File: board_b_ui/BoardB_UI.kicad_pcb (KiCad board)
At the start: 2 copper layers, 64 x 38 mm, 17 parts, among them J1 UI cable to Board A J6, J2 OLED SSD1306 I2C, SW1 EC11 encoder + push

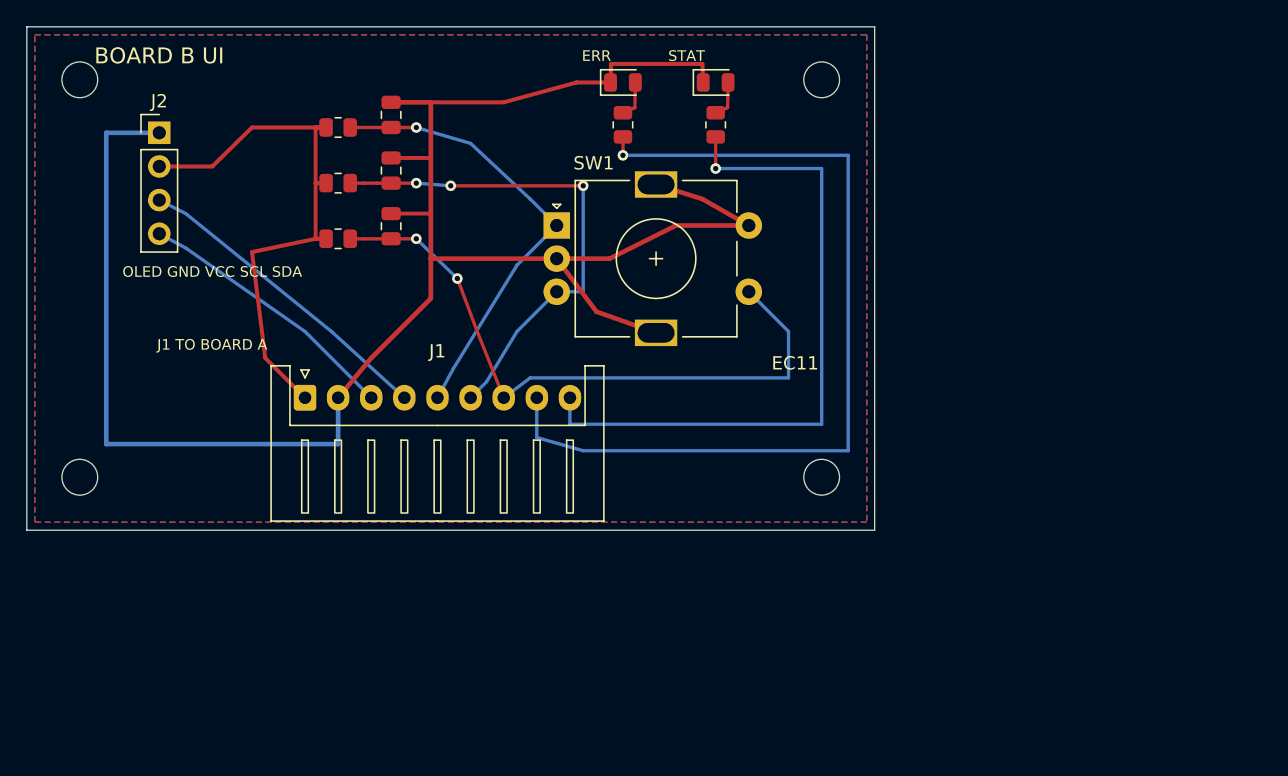
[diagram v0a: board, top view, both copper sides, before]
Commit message: Add Board B fab package and Board A hold report
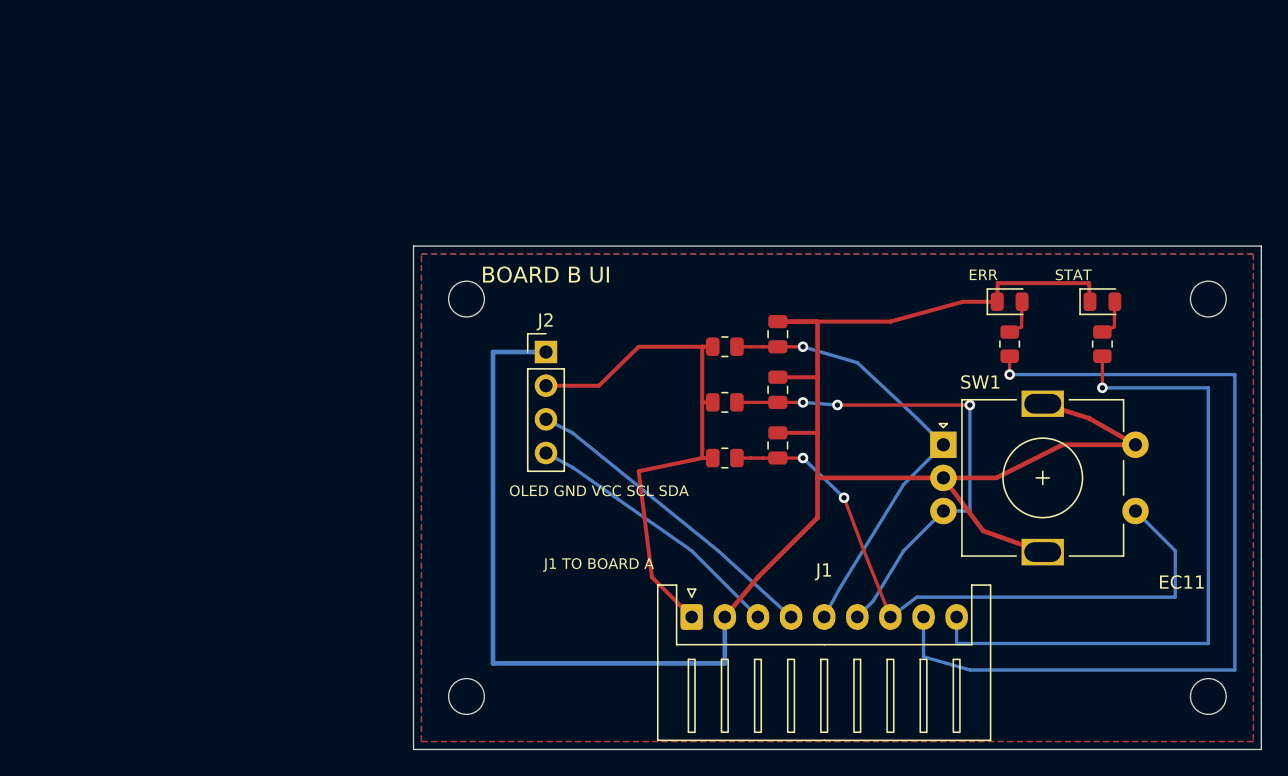
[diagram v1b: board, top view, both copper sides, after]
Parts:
- moved C1 33.6 mm to (56.7, 23.2)
- moved C2 33.6 mm to (56.7, 27.4)
- moved C3 33.6 mm to (56.7, 31.6)
- moved D1 33.6 mm to (74.2, 20.8)
- moved D2 33.6 mm to (81.2, 20.8)
- moved H1 33.6 mm to (33.2, 20.6)
- moved H2 33.6 mm to (89.2, 20.6)
- moved H3 33.6 mm to (33.2, 50.5)
- moved H4 33.6 mm to (89.2, 50.5)
- moved J1 33.6 mm to (50.2, 44.5)
- moved J2 33.6 mm to (39.2, 24.6)
- moved R1 33.6 mm to (52.7, 24.1)
- moved R2 33.6 mm to (52.7, 28.4)
- moved R3 33.6 mm to (52.7, 32.5)
- moved R4 33.6 mm to (74.2, 23.9)
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
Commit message: Clean up Board B front panel layout
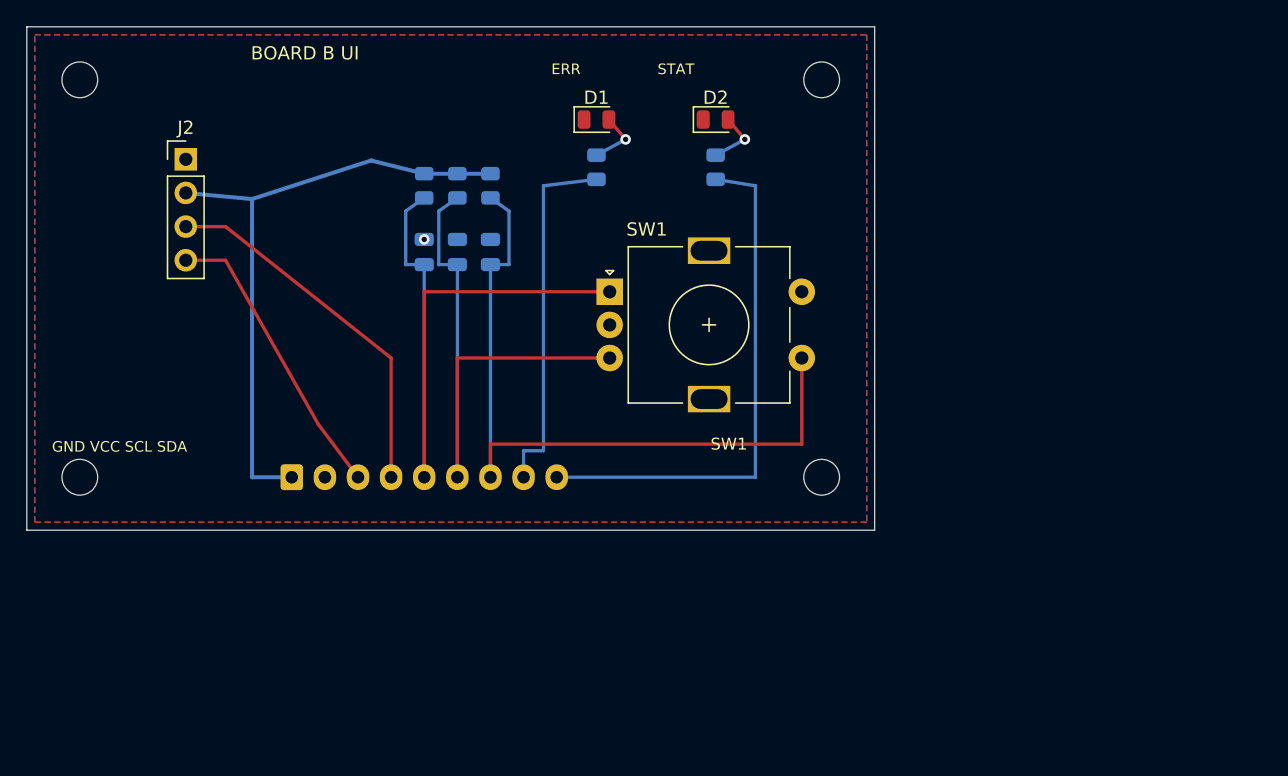
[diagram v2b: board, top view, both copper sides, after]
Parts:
- C1, C2, C3, J1, R1, R2, R3, R4, R5: moved to B.Cu
- moved D1 34.1 mm to (43.0, 7.00)
- moved R4 33.9 mm to (43.0, 10.6)
- moved H1 33.6 mm to (4.00, 4.00)
- moved H2 33.6 mm to (60.0, 4.00)
- moved H3 33.6 mm to (4.00, 34.0)
- moved H4 33.6 mm to (60.0, 34.0)
- moved D2 32.3 mm to (52.0, 7.00)
- moved R5 32.1 mm to (52.0, 10.6)
- moved J1 32.0 mm to (20.0, 34.0)
- moved J2 30.8 mm to (12.0, 10.0)
- moved SW1 27.7 mm to (44.0, 20.0)
- moved C1 27.4 mm to (30.0, 17.0)
- moved R3 27.1 mm to (35.0, 12.0), turned to -90 degrees
- moved C2 26.3 mm to (32.5, 17.0)
- moved C3 26.1 mm to (35.0, 17.0)
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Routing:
- net /GND: track 151.1 -> 0.00 mm, vias 0 -> 1
- net /ERROR_LED: track 67.3 -> 27.5 mm, vias 1 -> 0
- net /ENC_A: track 34.2 -> 51.2 mm, vias 1 -> 0
- net /STATUS_LED: track 50.7 -> 40.0 mm, vias 1 -> 0
- net /ENC_SW: track 48.7 -> 55.7 mm, vias 2 -> 0
- net /+3V3: track 41.8 -> 47.6 mm
- net /ENC_B: track 38.0 -> 43.7 mm, vias 3 -> 0
- net /SCL: track 23.8 -> 28.0 mm
- net /SDA: track 20.3 -> 22.2 mm
- net /STAT_LED_A: track 2.88 -> 4.46 mm, vias 0 -> 1
- net /ERR_LED_A: track 2.88 -> 4.46 mm, vias 0 -> 1
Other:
- board text added: "1=3V3 2=GND 3=SDA 4=SCL 5=A 6=B 7=SW 8=ERR 9=STAT"
- board text added: "GND VCC SCL SDA"
- board text added: "OLED 0.96 SSD1306"
- board text added: "SW1"
- board text removed: "EC11"
- board text removed: "J1 1=3V3 2=GND 3=SDA 4=SCL 5=A 6=B 7=SW 8=ERR 9=STAT"
- board text removed: "OLED GND VCC SCL SDA"

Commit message: Rebrand order package and add five-unit BOM
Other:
- board text added: "Self-Watering UI"
- board text removed: "BOARD B UI"
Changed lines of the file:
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@@
 		)
 	)
-	(gr_text "BOARD B UI"
+	(gr_text "Self-Watering UI"
 		(at 21 2 0)
 		(layer "F.SilkS")
